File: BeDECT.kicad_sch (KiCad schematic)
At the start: 29 parts, among them J1 EXP, J2 AudioJack3, SW1 SW_Push, U1 SC14CVMDECT

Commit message: update PCB
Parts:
- LS1: footprint (none) -> Connector_PinHeader_2.54mm:PinHeader_1x02_P2.54mm_Vertical
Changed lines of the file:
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@@
 			)
 		)
-		(property "Footprint" ""
+		(property "Footprint" "Connector_PinHeader_2.54mm:PinHeader_1x02_P2.54mm_Vertical"
 			(at 378.46 76.2 0)
 			(effects

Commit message: update PCB
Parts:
- added SW2, SW3, SW4: SW_Push, Button_Switch_SMD:SW_SPST_PTS647_Sx70, symbol Switch:SW_Push
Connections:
- net GND: now also SW2.1, SW3.1, SW4.1
- net Pi_GPIO22: now also SW2.2
- net Pi_GPIO23: now also SW3.2
- net Pi_GPIO24: now also SW4.2

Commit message: update pcb
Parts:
- SW2, SW3, SW4: footprint Button_Switch_SMD:SW_SPST_PTS647_Sx70 -> beepis:1TS003A-1800-3500A-CT
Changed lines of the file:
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@@
 			)
 		)
-		(property "Footprint" "Button_Switch_SMD:SW_SPST_PTS647_Sx70"
+		(property "Footprint" "beepis:1TS003A-1800-3500A-CT"
 			(at 186.69 71.12 0)
 			(effects
@@
 			)
 		)
-		(property "Footprint" "Button_Switch_SMD:SW_SPST_PTS647_Sx70"
+		(property "Footprint" "beepis:1TS003A-1800-3500A-CT"
 			(at 186.69 86.36 0)
 			(effects
@@
 			)
 		)
-		(property "Footprint" "Button_Switch_SMD:SW_SPST_PTS647_Sx70"
+		(property "Footprint" "beepis:1TS003A-1800-3500A-CT"
 			(at 186.69 78.74 0)
 			(effects

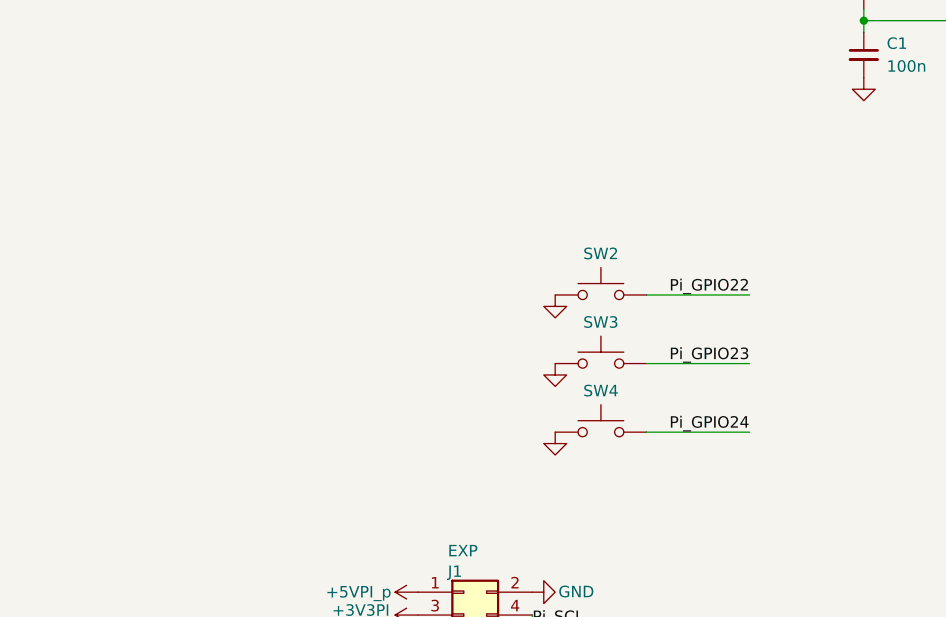
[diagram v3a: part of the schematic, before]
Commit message: Update PCB: Add button pullups
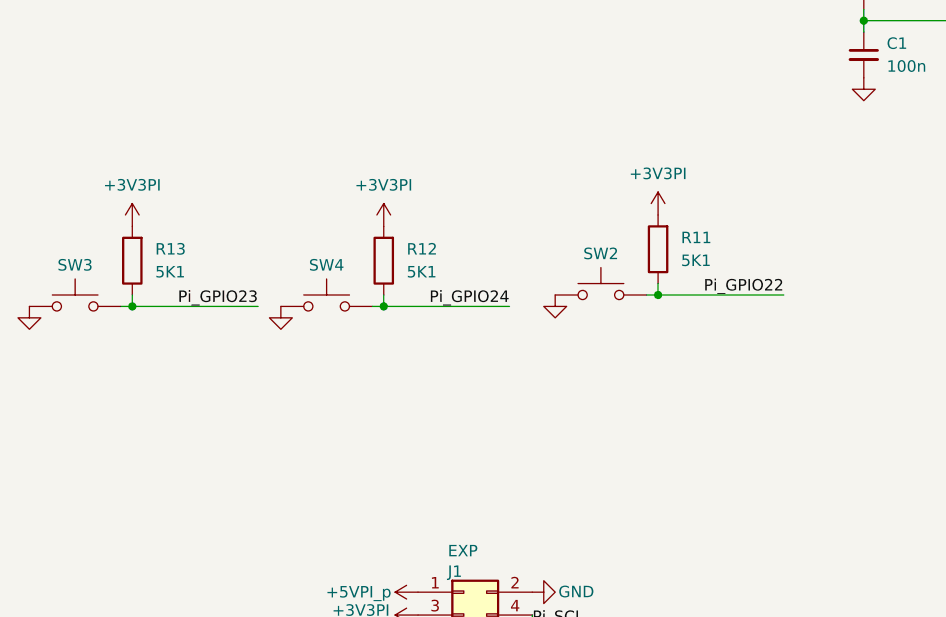
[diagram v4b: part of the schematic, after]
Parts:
- added R11, R12, R13: 5K1, Resistor_SMD:R_0603_1608Metric, symbol Device:R
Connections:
- net +3V3PI: now also R11.2, R12.2, R13.2
- net Pi_GPIO22: now also R11.1
- net Pi_GPIO23: now also R13.1
- net Pi_GPIO24: now also R12.1
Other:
- moved on the sheet: SW3, SW4

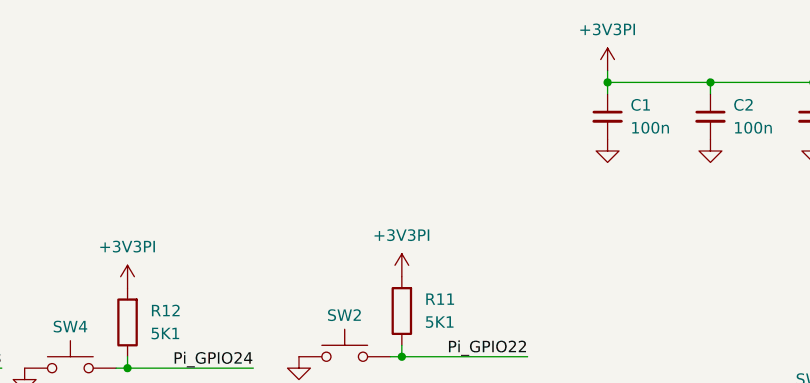
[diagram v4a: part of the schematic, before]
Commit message: Update PCB: via stitching, silkscreen
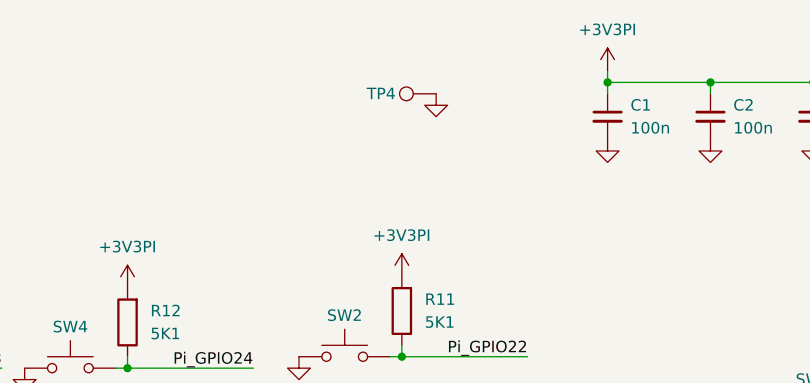
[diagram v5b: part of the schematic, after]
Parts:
- added TP4: TestPoint, TestPoint:TestPoint_Pad_D1.0mm, symbol Connector:TestPoint
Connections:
- net GND: now also TP4.1
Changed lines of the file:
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@@
+	)
+	(symbol
+		(lib_name "GND_1")
+		(lib_id "power:GND")
+		(at 196.85 46.99 0)
+		(unit 1)
+		(exclude_from_sim no)
+		(in_bom yes)
+		(on_board yes)
+		(dnp no)
+		(fields_autoplaced yes)
+		(property "Reference" "#PWR028"
+			(at 196.85 53.34 0)
+			(effects
+				(font
+					(size 1.27 1.27)
+				)
+				(hide yes)
+			)
+		)
+		(property "Value" "GND"
+			(at 196.85 52.07 0)
+			(effects
+				(font
+					(size 1.27 1.27)
+				)
+				(hide yes)
+			)
+		)
+		(property "Footprint" ""
+			(at 196.85 46.99 0)
+			(effects
+				(font
+					(size 1.27 1.27)
+				)
+				(hide yes)
+			)
+		)
+		(property "Datasheet" ""
+			(at 196.85 46.99 0)
+			(effects
+				(font
+					(size 1.27 1.27)
+				)
+				(hide yes)
+			)
+		)
+		(property "Description" "Power symbol creates a global label with name \"GND\" , ground"
+			(at 196.85 46.99 0)
+			(effects
+				(font
+					(size 1.27 1.27)
+				)
+				(hide yes)
+			)
+		)
+		(pin "1"
+		)
+		(instances
+			(project "BeDECT"
+				(path "/eb2713c5-b07c-450a-8da5-1de9bd273636"
+					(reference "#PWR028")
+					(unit 1)
+				)
+			)
+		)
 	)
 	(symbol
@@
 					(unit 1)
 				)
+			)
+		)
+	)
+	(symbol
+		(lib_id "Connector:TestPoint")
+		(at 196.85 46.99 90)
+		(unit 1)
+		(exclude_from_sim no)
+		(in_bom yes)
+		(on_board yes)
+		(dnp no)
+		(property "Reference" "TP4"
+			(at 190.754 46.99 90)
+			(effects
+				(font
+					(size 1.27 1.27)
+				)
+			)
+		)
+		(property "Value" "TestPoint"
+			(at 193.548 44.45 90)
+			(effects
+				(font
+					(size 1.27 1.27)
+				)
+				(hide yes)
+			)
+		)
+		(property "Footprint" "TestPoint:TestPoint_Pad_D1.0mm"
+			(at 196.85 41.91 0)
+			(effects
+				(font
+					(size 1.27 1.27)
+				)
+				(hide yes)
+			)
+		)
+		(property "Datasheet" "~"
+			(at 196.85 41.91 0)
+			(effects
+				(font
+					(size 1.27 1.27)
+				)
+				(hide yes)
+			)
+		)
+		(property "Description" "test point"
+			(at 196.85 46.99 0)
+			(effects
+				(font
+					(size 1.27 1.27)
+				)
+				(hide yes)
+			)
+		)
+		(pin "1"
+		)
+		(instances
+			(project "BeDECT"
+				(path "/eb2713c5-b07c-450a-8da5-1de9bd273636"
+					(reference "TP4")
+					(unit 1)
+				)

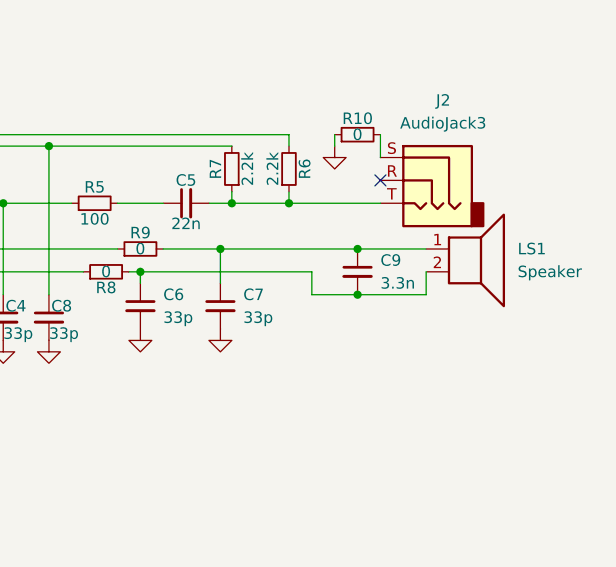
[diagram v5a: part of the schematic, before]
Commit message: Update Schematic: parallel speaker capacitor value
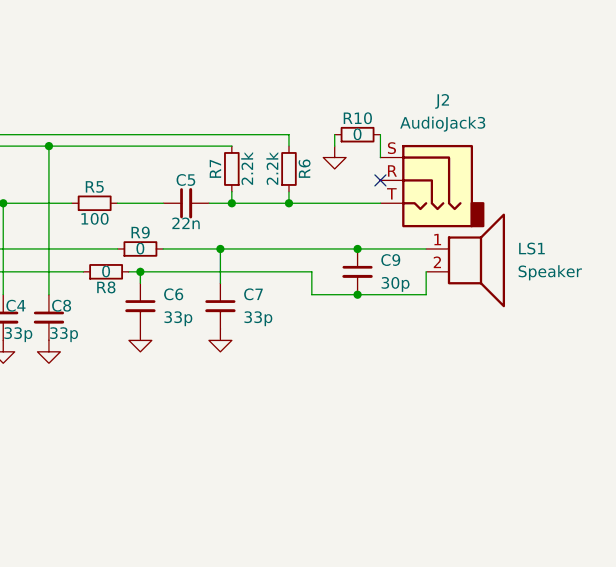
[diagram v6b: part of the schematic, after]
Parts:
- C9: value 3.3n -> 30p
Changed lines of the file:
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@@
 			)
 		)
-		(property "Value" "3.3n"
+		(property "Value" "30p"
 			(at 368.3 74.9362 0)
 			(effects
